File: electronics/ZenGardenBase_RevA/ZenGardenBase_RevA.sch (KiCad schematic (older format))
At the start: 26 parts, among them P1 Digital, P10 CONN_01X01, P11 CONN_01X01, P12 CONN_01X01, P13 CONN_01X01, P14 CONN_01X02, P2 Power, P3 Analog, P4 Analog, P5 PWM, P6 PWM, P7 Communication, P8 CONN_01X01, P9 CONN_01X01, Q1 2N7002, U1 NRF24L01+

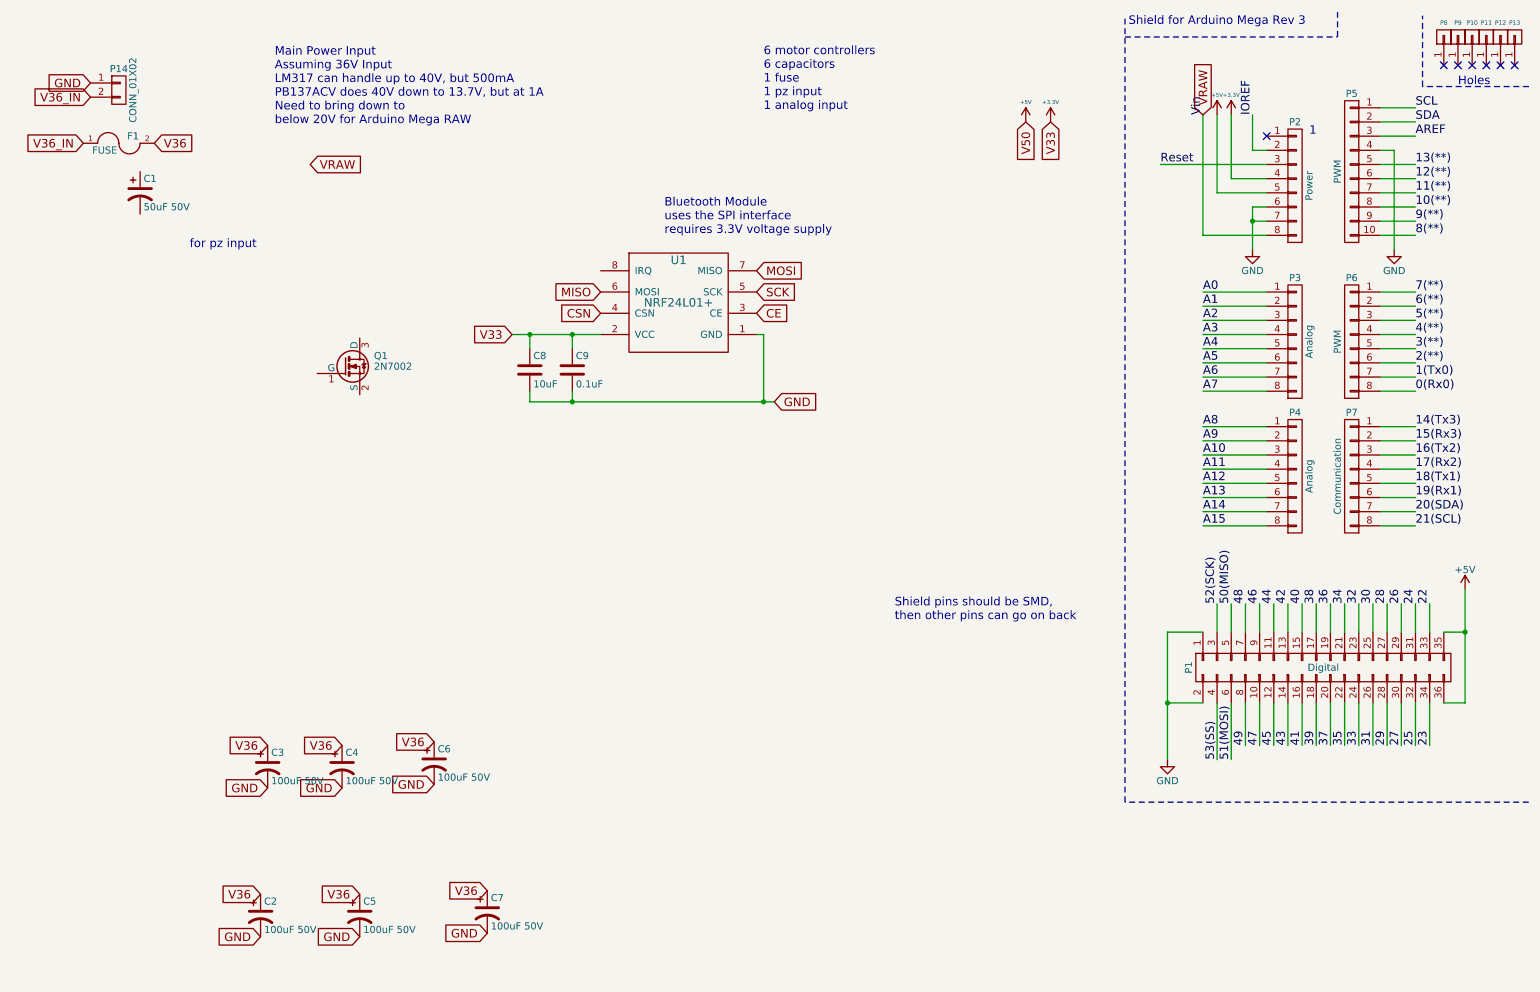
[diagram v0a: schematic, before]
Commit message: updated base schematic and layout to show that it will be easier to do on a breadboard
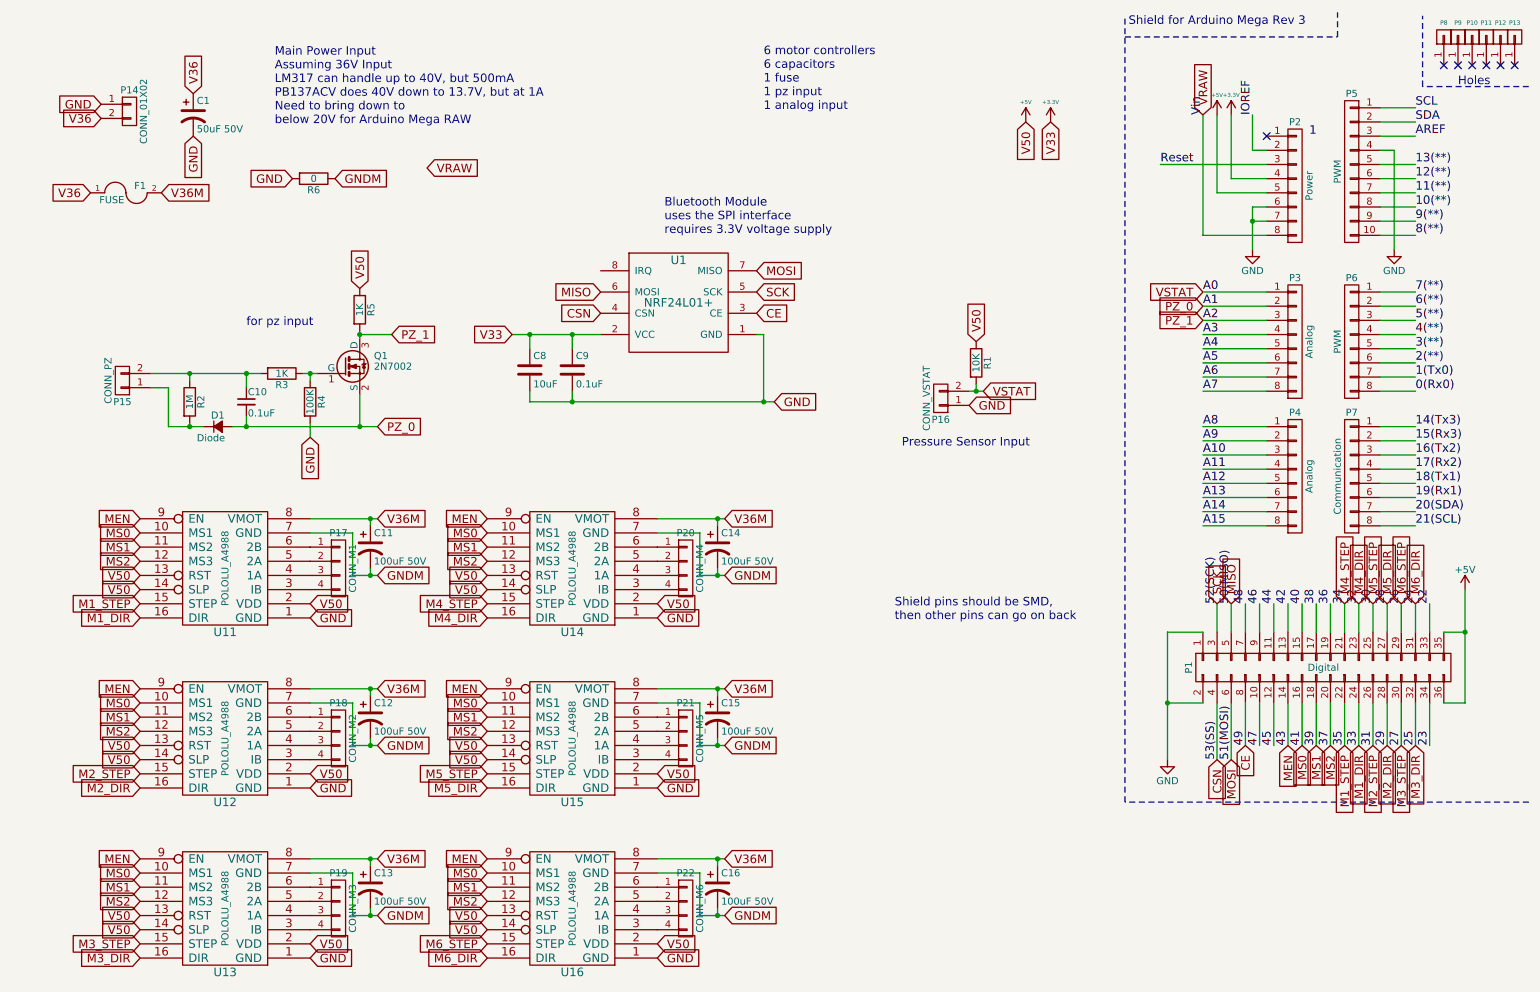
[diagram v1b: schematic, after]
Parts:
- removed C2, C4, C5, C6, C7: 100uF 50V, symbol CP1
- added C10: 0.1uF, Capacitors_SMD:C_0805, symbol C_Small
- added C12, C13, C14, C15, C16: 100uF 50V, Capacitors_ThroughHole:C_Radial_D8_L13_P3.8, symbol CP1
- added D1: Diode, Diodes_SMD:SOD-123, symbol D_Small
- added P15: CONN_PZ, Pin_Headers:Pin_Header_Straight_1x02, symbol CONN_01X02
- added P16: CONN_VSTAT, Pin_Headers:Pin_Header_Straight_1x02, symbol CONN_01X02
- added P17: CONN_M1, Connect:AK300-4, symbol CONN_01X04
- added P18: CONN_M2, Connect:AK300-4, symbol CONN_01X04
- added P19: CONN_M3, Connect:AK300-4, symbol CONN_01X04
- added P20: CONN_M4, Connect:AK300-4, symbol CONN_01X04
- added P21: CONN_M5, Connect:AK300-4, symbol CONN_01X04
- added P22: CONN_M6, Connect:AK300-4, symbol CONN_01X04
- added R1: 10K, Resistors_SMD:R_1206, symbol R
- added R2: 1M, Resistors_SMD:R_1206, symbol R
- added R3, R5: 1K, Resistors_SMD:R_1206, symbol R
- added R4: 100K, Resistors_SMD:R_1206, symbol R
- added R6: 0, Resistors_SMD:R_1206, symbol R
- added U11, U12, U13, U14, U15, U16: POLOLU_A4988, MyKiCadParts:SWDIP8_.6W, symbol POLOLU_A4988
- C1: footprint (none) -> Capacitors_ThroughHole:C_Radial_D6.3_L11.2_P2.5
- C11: renamed from C3; footprint (none) -> Capacitors_ThroughHole:C_Radial_D8_L13_P3.8
- C8: footprint (none) -> Capacitors_SMD:C_1206
- C9: footprint (none) -> Capacitors_SMD:C_0805
- F1: footprint (none) -> Fuse_Holders_and_Fuses:Fuse_TE5_Littlefuse-395Series
- P14: footprint (none) -> Connect:AK300-2
- U1: footprint (none) -> MyKiCadParts:NRF24L01+
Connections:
- net 49 is gone; now on net CE: P1.8 (P8)
- net 50(MISO) is gone; now on net MISO: P1.5 (P5)
- net 51(MOSI) is gone; now on net MOSI: P1.6 (P6)
- net 52(SCK) is gone; now on net SCK: P1.3 (P3)
- net 53(SS) is gone; now on net CSN: P1.4 (P4)
- net A1 is gone; now on net PZ_0: P3.2 (P2)
- net A2 is gone; now on net PZ_1: P3.3 (P3)
- net V36_IN is gone; now on net V36: F1.1, P14.2 (P2)
- net +5V: now also R1.1, R5.1, U11.13 (RST), U11.14 (SLP), U11.2 (VDD), U12.13 (RST), U12.14 (SLP), U12.2 (VDD), U13.13 (RST), U13.14 (SLP), U13.2 (VDD), U14.13 (RST), U14.14 (SLP), U14.2 (VDD), U15.13 (RST), U15.14 (SLP), U15.2 (VDD), U16.13 (RST), U16.14 (SLP), U16.2 (VDD)
- net GND: now also C1.2, P16.1 (P1), R4.2, R6.2, U11.1 (GND), U12.1 (GND), U13.1 (GND), U14.1 (GND), U15.1 (GND), U16.1 (GND); no longer C11.2
- net V36: now also C1.1; no longer C11.1, F1.2
- net at Q1.1 (G): now also R3.1, R4.1
- net PZ_0: now reaches Q1.2 (S)
- net PZ_0: now also C10.2, D1.2 (A)
- net PZ_1: now reaches Q1.3 (D)
- net PZ_1: now also R5.2
- net 24 renamed M6_DIR
- net M6_DIR: now also U16.16 (DIR)
- net 25 renamed M3_DIR
- net M3_DIR: now also U13.16 (DIR)
- net 26 renamed M6_STEP
- net M6_STEP: now also U16.15 (STEP)
- net 27 renamed M3_STEP
- net M3_STEP: now also U13.15 (STEP)
- net 28 renamed M5_DIR
- net M5_DIR: now also U15.16 (DIR)
- net 29 renamed M2_DIR
- net M2_DIR: now also U12.16 (DIR)
- net 30 renamed M5_STEP
- net M5_STEP: now also U15.15 (STEP)
- net 31 renamed M2_STEP
- net M2_STEP: now also U12.15 (STEP)
- net 32 renamed M4_DIR
- net M4_DIR: now also U14.16 (DIR)
- net 33 renamed M1_DIR
- net M1_DIR: now also U11.16 (DIR)
- net 34 renamed M4_STEP
- net M4_STEP: now also U14.15 (STEP)
- net 35 renamed M1_STEP
- net M1_STEP: now also U11.15 (STEP)
- net 37 renamed MS2
- net MS2: now also U11.12 (MS3), U12.12 (MS3), U13.12 (MS3), U14.12 (MS3), U15.12 (MS3), U16.12 (MS3)
- net 39 renamed MS1
- net MS1: now also U11.11 (MS2), U12.11 (MS2), U13.11 (MS2), U14.11 (MS2), U15.11 (MS2), U16.11 (MS2)
- net 41 renamed MS0
- net MS0: now also U11.10 (MS1), U12.10 (MS1), U13.10 (MS1), U14.10 (MS1), U15.10 (MS1), U16.10 (MS1)
- net 43 renamed MEN
- net MEN: now also U11.9 (EN), U12.9 (EN), U13.9 (EN), U14.9 (EN), U15.9 (EN), U16.9 (EN)
- net A0 renamed VSTAT
- net VSTAT: now also P16.2 (P2), R1.2
- new net: D1.1 (K), P15.1 (P1), R2.2
- new net: C10.1, P15.2 (P2), R2.1, R3.2
- new net: P17.4 (P4), U11.3 (IB)
- new net: P17.3 (P3), U11.4 (1A)
- new net: P17.2 (P2), U11.5 (2A)
- new net: P17.1 (P1), U11.6 (2B)
- new net: P18.4 (P4), U12.3 (IB)
- new net: P18.3 (P3), U12.4 (1A)
- new net: P18.2 (P2), U12.5 (2A)
- new net: P18.1 (P1), U12.6 (2B)
- new net: P20.4 (P4), U14.3 (IB)
- new net: P20.3 (P3), U14.4 (1A)
- new net: P20.2 (P2), U14.5 (2A)
- new net: P20.1 (P1), U14.6 (2B)
- new net: P21.4 (P4), U15.3 (IB)
- new net: P21.3 (P3), U15.4 (1A)
- new net: P21.2 (P2), U15.5 (2A)
- new net: P21.1 (P1), U15.6 (2B)
- new net: P19.4 (P4), U13.3 (IB)
- new net: P19.3 (P3), U13.4 (1A)
- new net: P19.2 (P2), U13.5 (2A)
- new net: P19.1 (P1), U13.6 (2B)
- new net: P22.4 (P4), U16.3 (IB)
- new net: P22.3 (P3), U16.4 (1A)
- new net: P22.2 (P2), U16.5 (2A)
- new net: P22.1 (P1), U16.6 (2B)
- new net GNDM: C11.2, C12.2, C13.2, C14.2, C15.2, C16.2, R6.1, U11.7 (GND), U12.7 (GND), U13.7 (GND), U14.7 (GND), U15.7 (GND), U16.7 (GND)
- new net V36M: C11.1, C12.1, C13.1, C14.1, C15.1, C16.1, F1.2, U11.8 (VMOT), U12.8 (VMOT), U13.8 (VMOT), U14.8 (VMOT), U15.8 (VMOT), U16.8 (VMOT)
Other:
- note added: "Pressure Sensor Input"
- moved on the sheet: C1, C11, F1, P14
